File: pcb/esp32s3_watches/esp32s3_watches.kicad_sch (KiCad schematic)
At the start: 0 parts

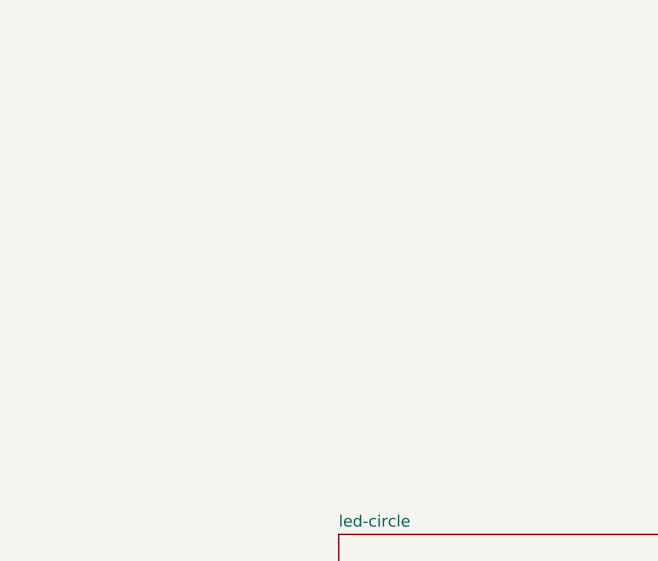
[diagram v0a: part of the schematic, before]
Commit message: Update SD card connection
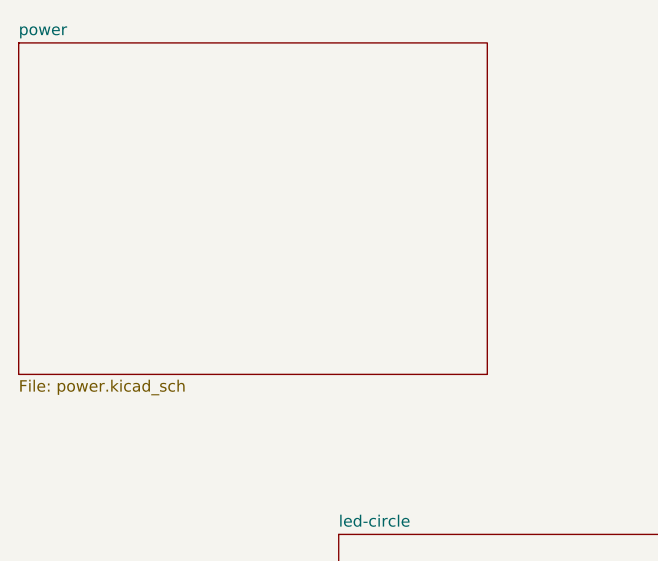
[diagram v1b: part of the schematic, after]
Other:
- added sheet power (power.kicad_sch)
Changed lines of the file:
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@@
+		)
+	)
+	(sheet
+		(at 36.83 22.86)
+		(size 52.07 36.83)
+		(fields_autoplaced yes)
+		(stroke
+			(width 0.1524)
+			(type solid)
+		)
+		(fill
+			(color 0 0 0 0.0000)
+		)
+		(property "Sheetname" "power"
+			(at 36.83 22.1484 0)
+			(effects
+				(font
+					(size 1.27 1.27)
+				)
+				(justify left bottom)
+			)
+		)
+		(property "Sheetfile" "power.kicad_sch"
+			(at 36.83 60.2746 0)
+			(effects
+				(font
+					(size 1.27 1.27)
+				)
+				(justify left top)
+			)
+		)
+		(instances
+			(project "esp32s3_watches"
+				(path "/546746d8-9087-4747-b922-4ea0efc98497"
+					(page "4")
+				)
+			)
 		)
 	)

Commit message: Scheme improvements
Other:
- added sheet PCF8563 (PCF8563.kicad_sch)
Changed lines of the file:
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@@
 	(paper "A4")
 	(sheet
-		(at 72.39 77.47)
-		(size 35.56 36.83)
+		(at 101.6 25.4)
+		(size 25.4 25.4)
 		(fields_autoplaced yes)
 		(stroke
@@
 		)
 		(property "Sheetname" "led-circle"
-			(at 72.39 76.7584 0)
+			(at 101.6 24.6884 0)
 			(effects
 				(font
@@
 		)
 		(property "Sheetfile" "led-circle.kicad_sch"
-			(at 72.39 114.8846 0)
+			(at 101.6 51.3846 0)
 			(effects
 				(font
@@
 	)
 	(sheet
-		(at 96.52 138.43)
-		(size 38.1 34.29)
+		(at 63.5 25.4)
+		(size 25.4 25.4)
 		(fields_autoplaced yes)
 		(stroke
@@
 		)
 		(property "Sheetname" "esp32-s3"
-			(at 96.52 137.7184 0)
+			(at 63.5 24.6884 0)
 			(effects
 				(font
@@
 		)
 		(property "Sheetfile" "esp32-s3.kicad_sch"
-			(at 96.52 173.3046 0)
+			(at 63.5 51.3846 0)
 			(effects
 				(font
@@
 	)
 	(sheet
-		(at 36.83 22.86)
-		(size 52.07 36.83)
+		(at 139.7 25.4)
+		(size 25.4 25.4)
+		(fields_autoplaced yes)
+		(stroke
+			(width 0.1524)
+			(type solid)
+		)
+		(fill
+			(color 0 0 0 0.0000)
+		)
+		(property "Sheetname" "PCF8563"
+			(at 139.7 24.6884 0)
+			(effects
+				(font
+					(size 1.27 1.27)
+				)
+				(justify left bottom)
+			)
+		)
+		(property "Sheetfile" "PCF8563.kicad_sch"
+			(at 139.7 51.3846 0)
+			(effects
+				(font
+					(size 1.27 1.27)
+				)
+				(justify left top)
+			)
+		)
+		(instances
+			(project "esp32s3_watches"
+				(path "/546746d8-9087-4747-b922-4ea0efc98497"
+					(page "5")
+				)
+			)
+		)
+	)
+	(sheet
+		(at 25.4 25.4)
+		(size 25.4 25.4)
 		(fields_autoplaced yes)
 		(stroke
@@
 		)
 		(property "Sheetname" "power"
-			(at 36.83 22.1484 0)
+			(at 25.4 24.6884 0)
 			(effects
 				(font
@@
 		)
 		(property "Sheetfile" "power.kicad_sch"
-			(at 36.83 60.2746 0)
+			(at 25.4 51.3846 0)
 			(effects
 				(font

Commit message: minor PCB updates
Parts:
- added H1, H2, H3, H4: MountingHole, MountingHole:MountingHole_3.2mm_M3, symbol Mechanical:MountingHole
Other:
- note added: "Mounting Holes (M3)"

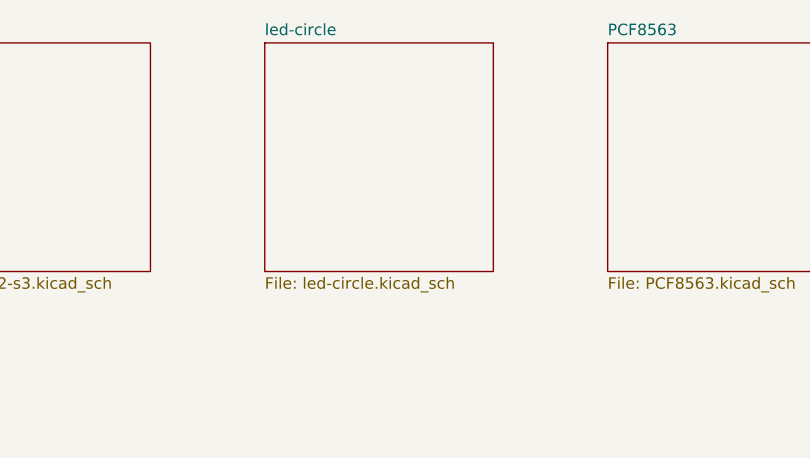
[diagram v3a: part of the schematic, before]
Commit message: Split scheme to 2 boards
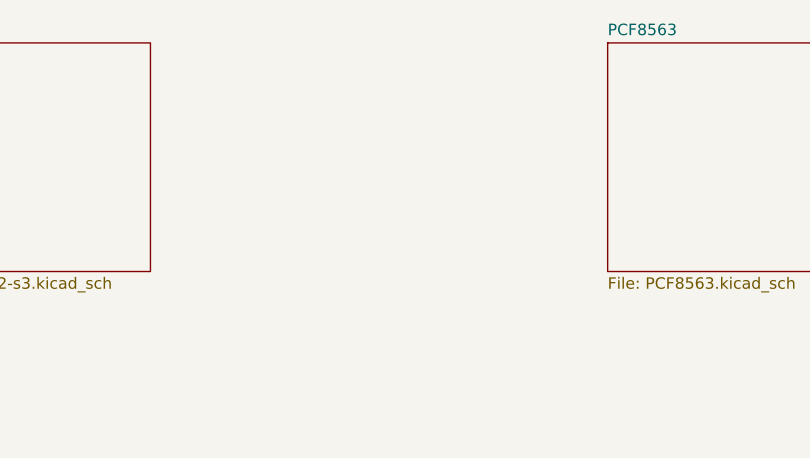
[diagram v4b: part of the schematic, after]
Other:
- removed sheet led-circle
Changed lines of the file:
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@@
-	)
-	(sheet
-		(at 101.6 25.4)
-		(size 25.4 25.4)
-		(fields_autoplaced yes)
-		(stroke
-			(width 0.1524)
-			(type solid)
-		)
-		(fill
-			(color 0 0 0 0.0000)
-		)
-		(property "Sheetname" "led-circle"
-			(at 101.6 24.6884 0)
-			(effects
-				(font
-					(size 1.27 1.27)
-				)
-				(justify left bottom)
-			)
-		)
-		(property "Sheetfile" "led-circle.kicad_sch"
-			(at 101.6 51.3846 0)
-			(effects
-				(font
-					(size 1.27 1.27)
-				)
-				(justify left top)
-			)
-		)
-		(instances
-			(project "esp32s3_watches"
-				(path "/546746d8-9087-4747-b922-4ea0efc98497"
-					(page "3")
-				)
-			)
-		)
 	)
 	(sheet
